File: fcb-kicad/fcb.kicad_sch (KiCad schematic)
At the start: 50 parts, among them J1 Conn_ESC_4in1, J2 SWD, SW1 SW_Push, SW2 SW_SPDT, U1 TPS5430DDA, U2 AMS1117-3.3, U5 STM32F411CEUx, Y1 16 MHz

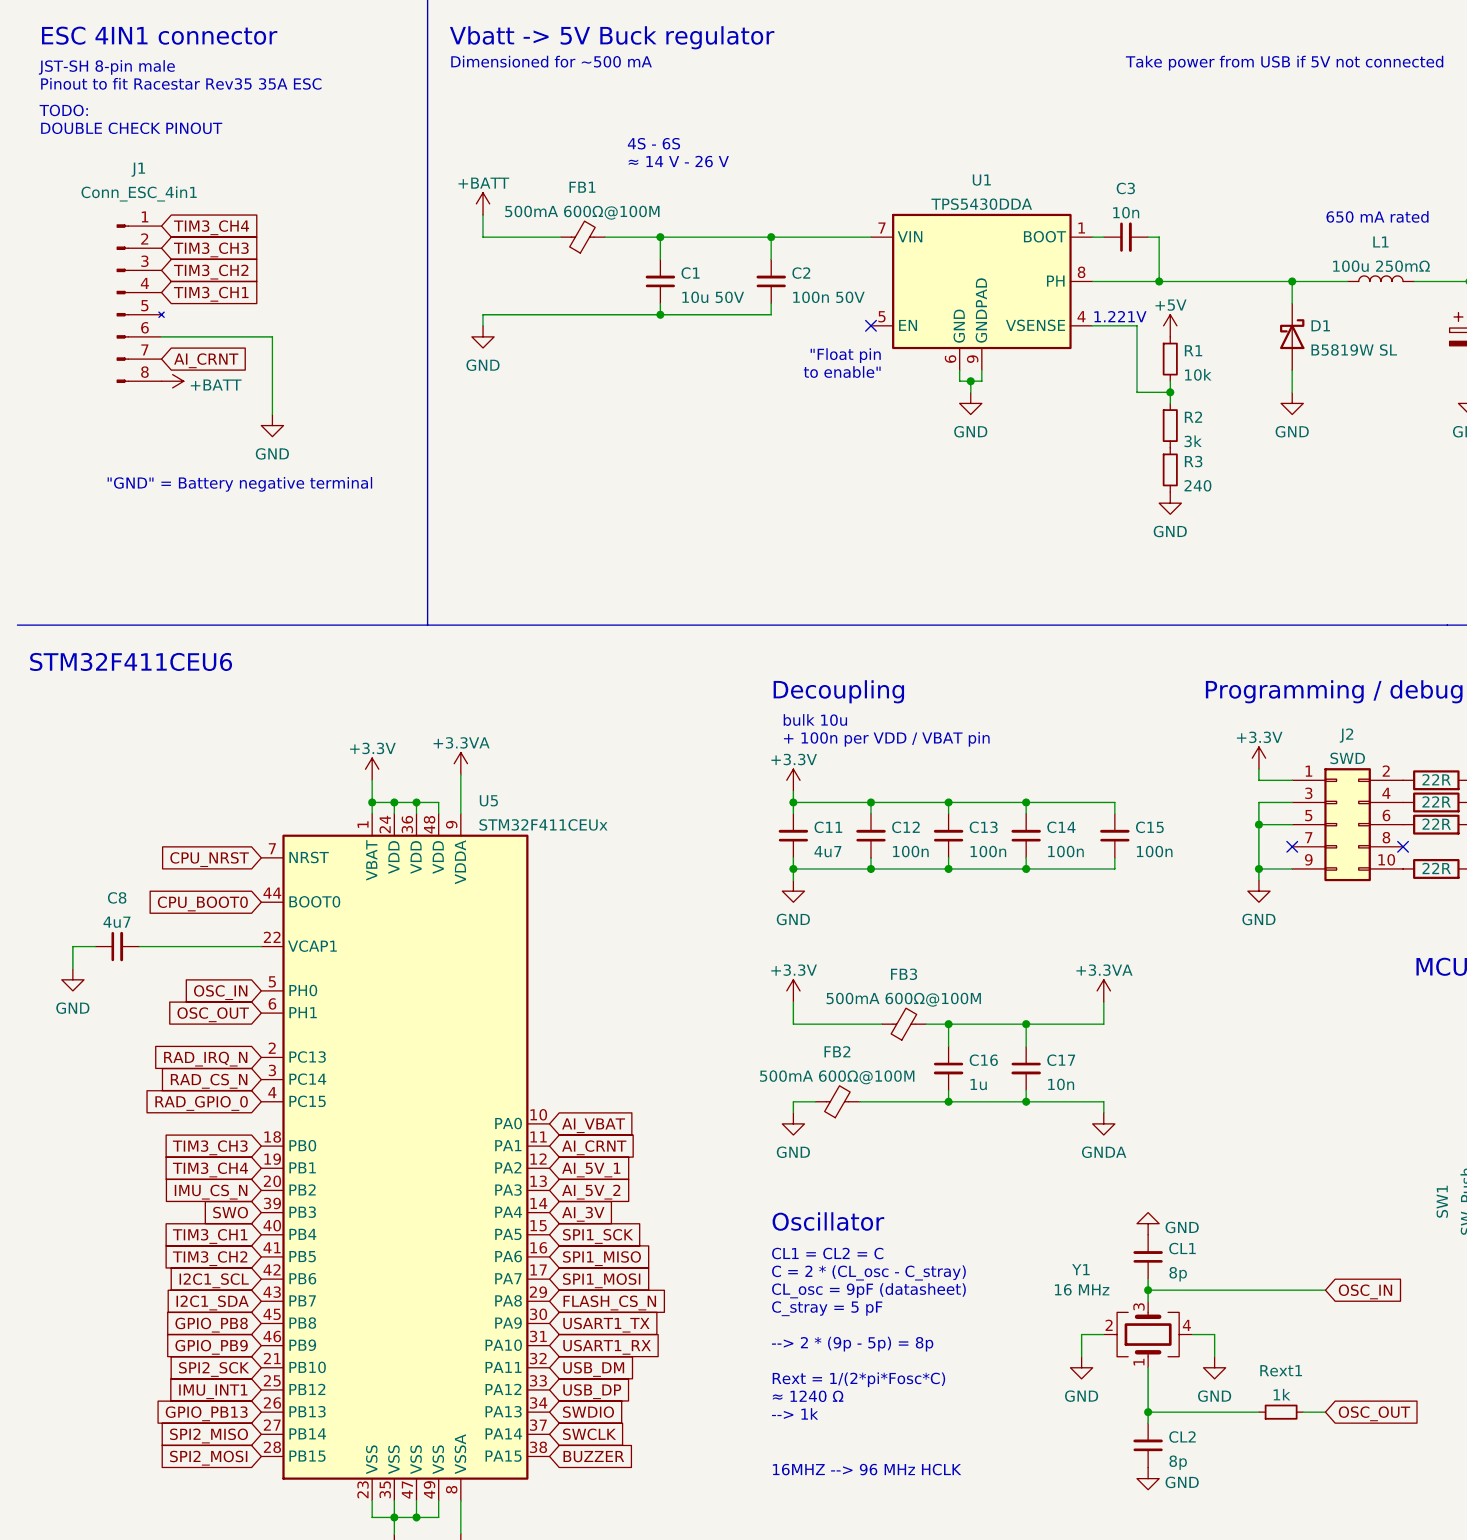
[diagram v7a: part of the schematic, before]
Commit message: Analog inputs, connectors to GPIO
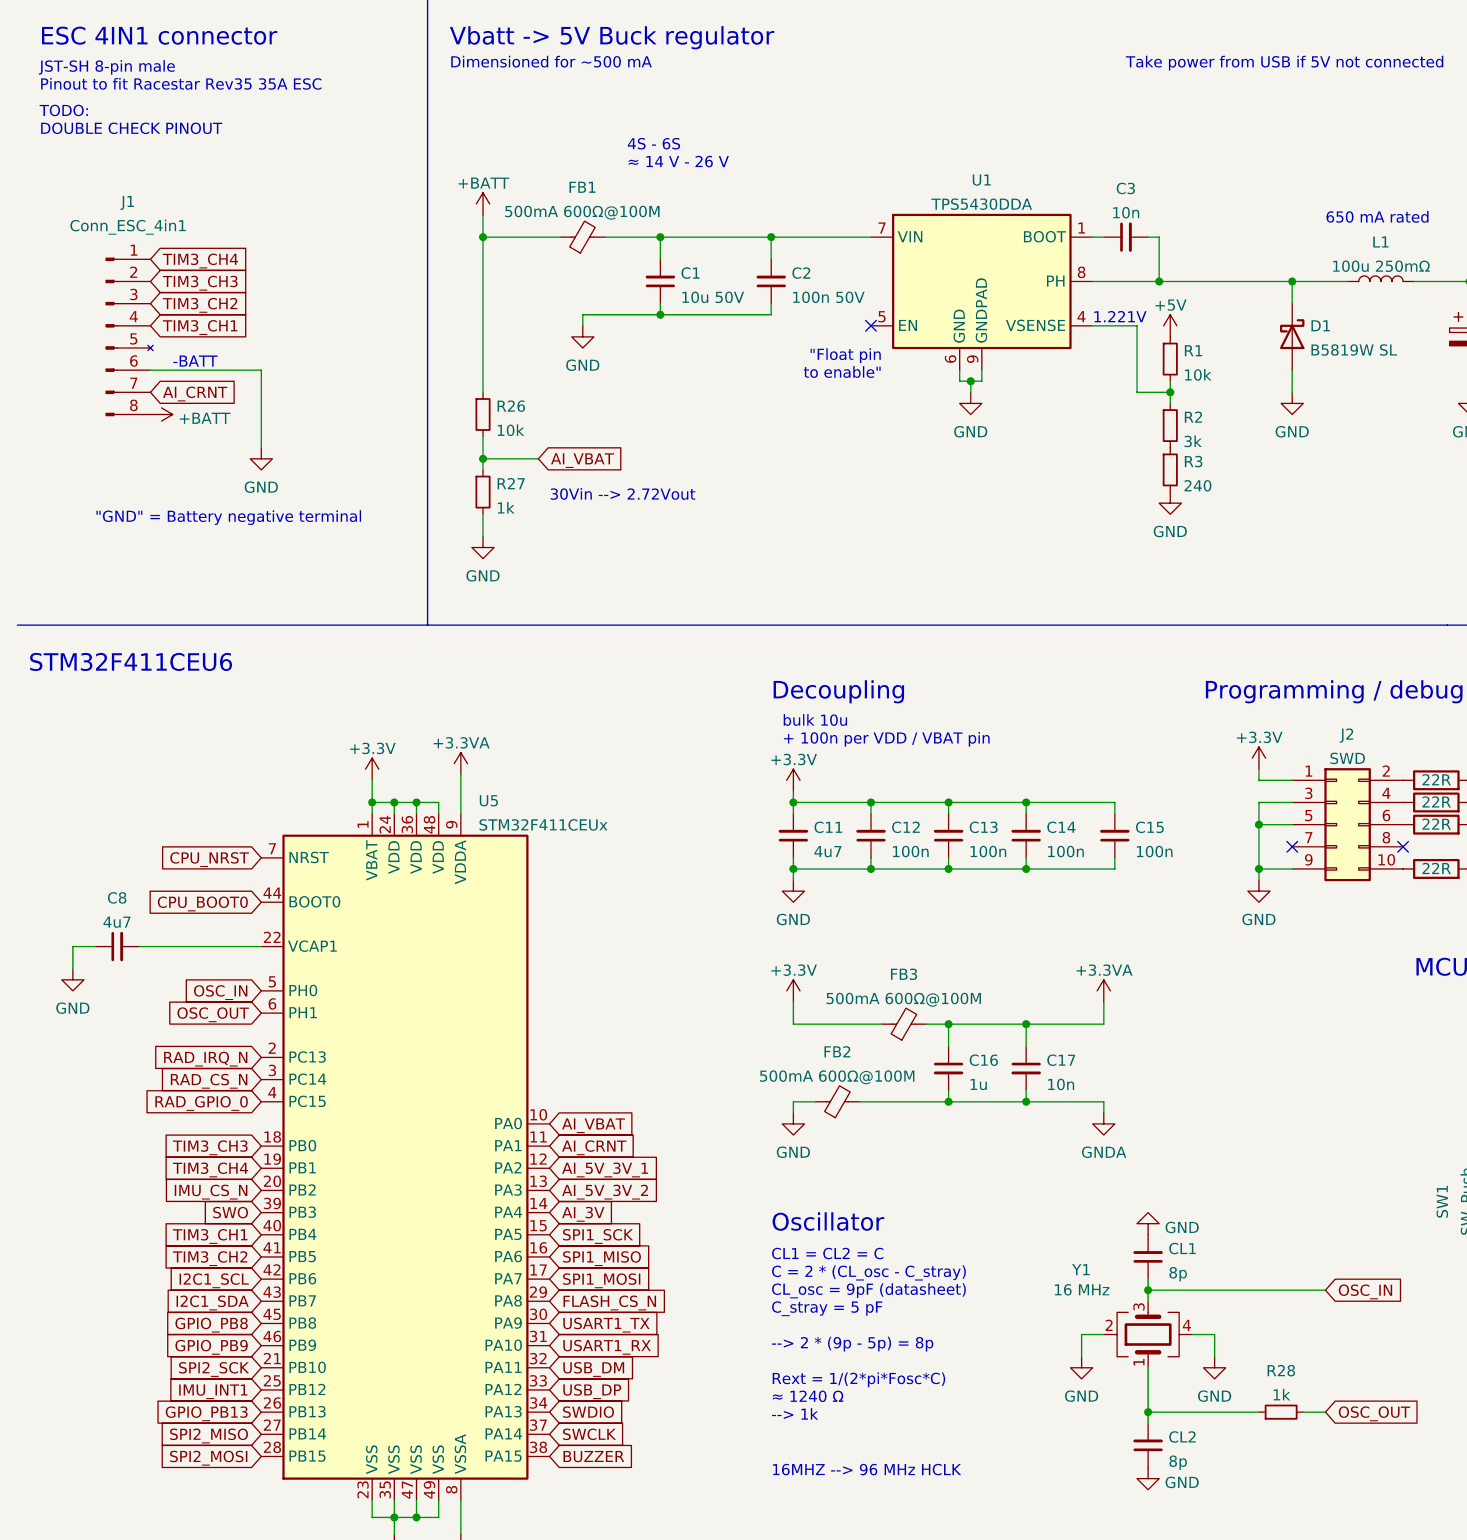
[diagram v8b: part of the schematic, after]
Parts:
- added R26: 10k, Resistor_SMD:R_0603_1608Metric, symbol Device:R_Small
- added R27: 1k, symbol Device:R_Small
- renumbered Rext1 to R28
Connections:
- net +BATT: now also R26.1
- net AI_VBAT: now also R26.2, R27.1
- net GND: now also R27.2
- net AI_5V_1 renamed AI_5V_3V_1
- net AI_5V_2 renamed AI_5V_3V_2
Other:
- note added: "-BATT"
- note added: "30Vin --> 2.72Vout"
- moved on the sheet: J1
